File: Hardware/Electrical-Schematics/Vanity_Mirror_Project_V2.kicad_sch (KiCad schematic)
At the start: 41 parts, among them IC1 SN74LV1T34QDBVRQ1, IC2 FDC1004QDGSRQ1, J1 USB_C_Receptacle_USB2.0_14P, Q1 Q_NPN_BEC, Q2 Q_NPN_BEC, SW1 RST, U1 CH340C, U2 ESP-12F, U3 USBLC6-2SC6, U4 XL1509-3.3

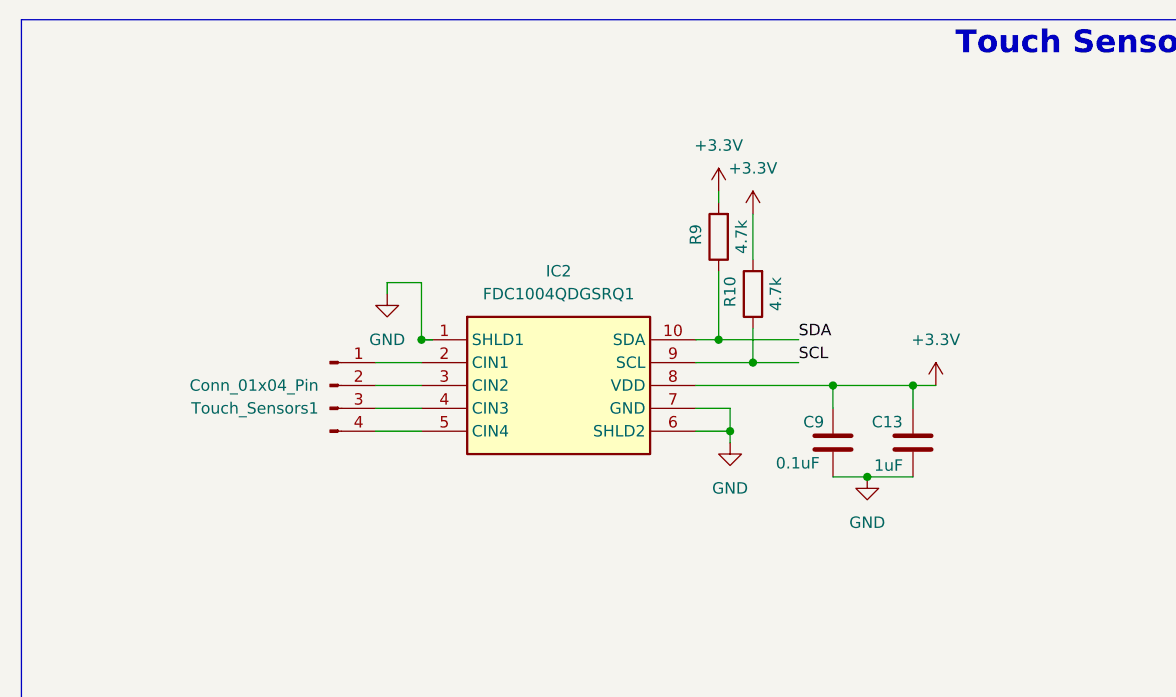
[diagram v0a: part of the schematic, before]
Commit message: Cleaning files
Switching Kicad versions and switching laptops
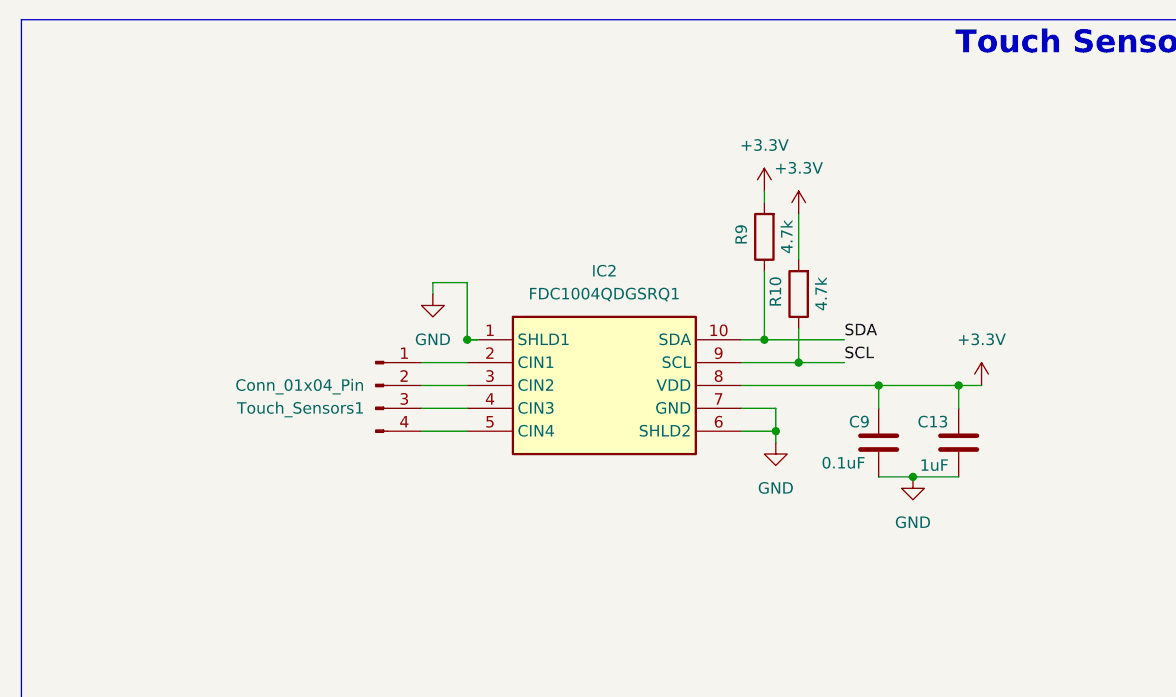
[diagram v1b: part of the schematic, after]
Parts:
- C10, C12: footprint Capacitor_Tantalum_SMD:CP_EIA-7343-31_Kemet-D_HandSolder -> Capacitor_THT:CP_Radial_D8.0mm_P3.50mm
- IC2: footprint VanityMirror_FootPrints:SOP50P490X110-10N -> SOP50P490X110-10N
- L2: footprint VanityMirror_FootPrints:INDPM110100X400N -> INDPM110100X400N
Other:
- moved on the sheet: C13, C9, IC2, R10, R9, Touch_Sensors1
